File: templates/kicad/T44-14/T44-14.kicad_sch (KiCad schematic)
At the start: 14 parts

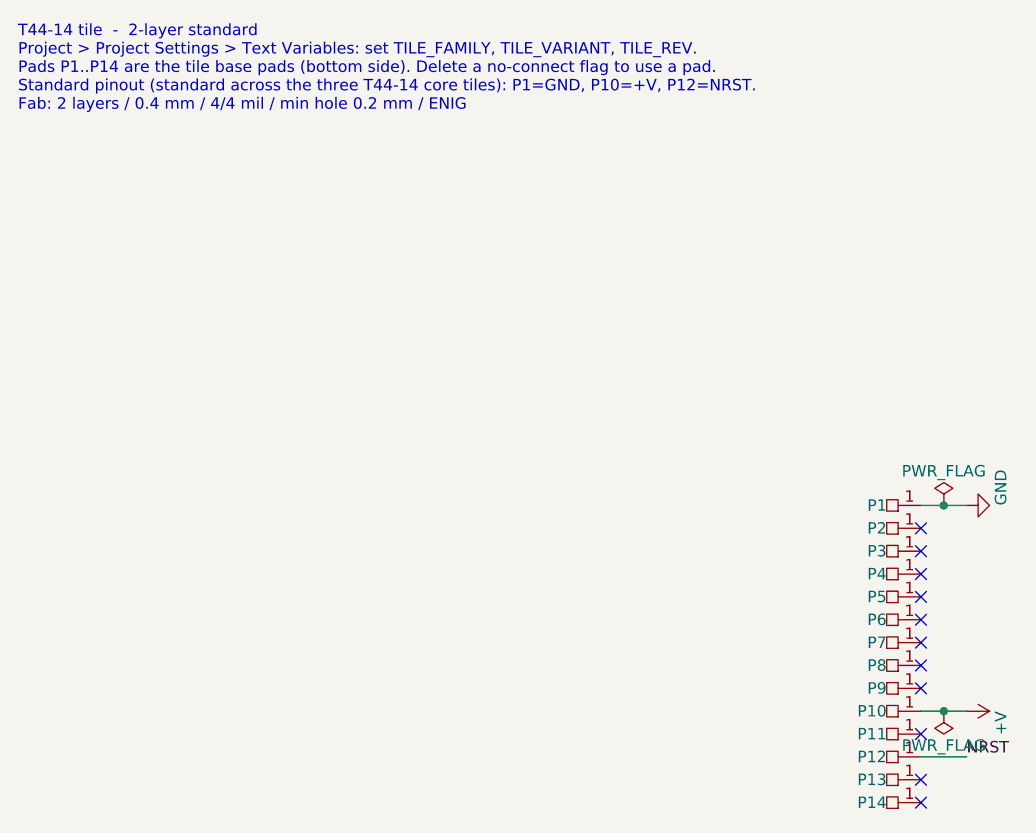
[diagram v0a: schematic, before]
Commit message: Re-tier on measured prices: 4L on 0.2 mm drill, add 4L-fine
4L keeps the 0.2 mm drill so it lands in PCBWay's $162 standard bucket
rather than the $419 one; 3/3 mil and 0.15 mm drills move to a new 4L-fine
tier on the advanced form. Quotes name the calculator to use. set_tier.py
gains --package for projects that predate the templates and --ignore-locks
for stale lock files.

Co-Authored-By: Claude Fable 5.1 <noreply@anthropic.com>
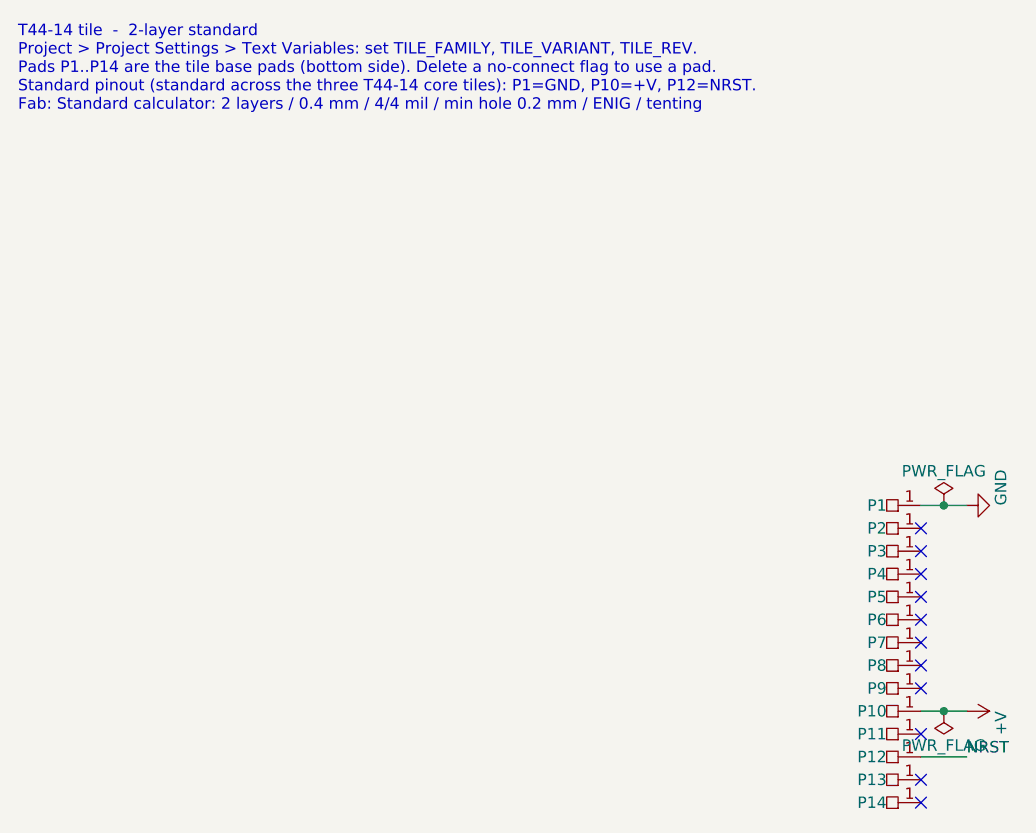
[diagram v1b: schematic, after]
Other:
- note added: "T44-14 tile - 2-layer standard Project > Project Settings > Text Variables: set TILE_FAMILY, TILE_VARIANT, TILE_REV. Pads P1..P14 are the tile base pads (bottom side). Delete a no-connect flag to use a pad. Standard pinout (standard across the three T44-14 core tiles): P1=GND, P10=+V, P12=NRST. Fab: Standard calculator: 2 layers / 0.4 mm / 4/4 mil / min hole 0.2 mm / ENIG / tenting"
- note removed: "T44-14 tile - 2-layer standard Project > Project Settings > Text Variables: set TILE_FAMILY, TILE_VARIANT, TILE_REV. Pads P1..P14 are the tile base pads (bottom side). Delete a no-connect flag to use a pad. Standard pinout (standard across the three T44-14 core tiles): P1=GND, P10=+V, P12=NRST. Fab: 2 layers / 0.4 mm / 4/4 mil / min hole 0.2 mm / ENIG"
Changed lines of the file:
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@@
 		(comment 2 "${FAB_QUOTE}")
 	)
-	(text "T44-14 tile  -  2-layer standard\nProject > Project Settings > Text Variables: set TILE_FAMILY, TILE_VARIANT, TILE_REV.\nPads P1..P14 are the tile base pads (bottom side). Delete a no-connect flag to use a pad.\nStandard pinout (standard across the three T44-14 core tiles): P1=GND, P10=+V, P12=NRST.\nFab: 2 layers / 0.4 mm / 4/4 mil / min hole 0.2 mm / ENIG"
+	(text "T44-14 tile  -  2-layer standard\nProject > Project Settings > Text Variables: set TILE_FAMILY, TILE_VARIANT, TILE_REV.\nPads P1..P14 are the tile base pads (bottom side). Delete a no-connect flag to use a pad.\nStandard pinout (standard across the three T44-14 core tiles): P1=GND, P10=+V, P12=NRST.\nFab: Standard calculator: 2 layers / 0.4 mm / 4/4 mil / min hole 0.2 mm / ENIG / tenting"
 		(exclude_from_sim no)
 		(at 25.4 25.4 0)
